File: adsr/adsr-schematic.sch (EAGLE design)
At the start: 28 parts, among them IC1 NE555N, IC2 LM358N, Q1 BC548B, Q2 BC548B, Q3 BC548B

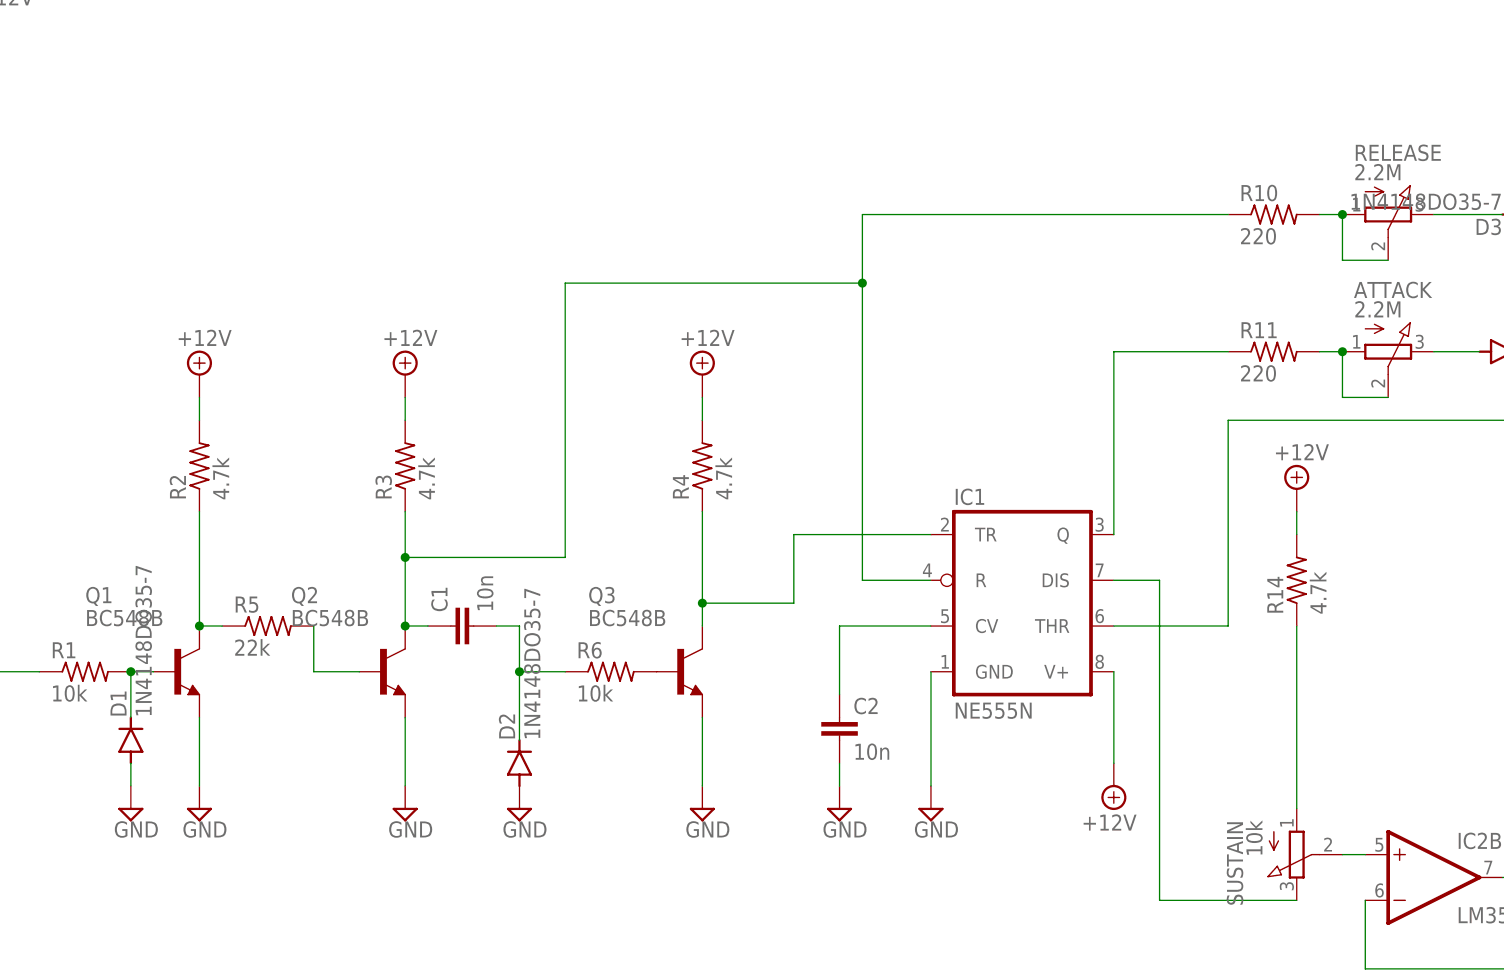
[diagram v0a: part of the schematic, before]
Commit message: save sequencer and adsr.
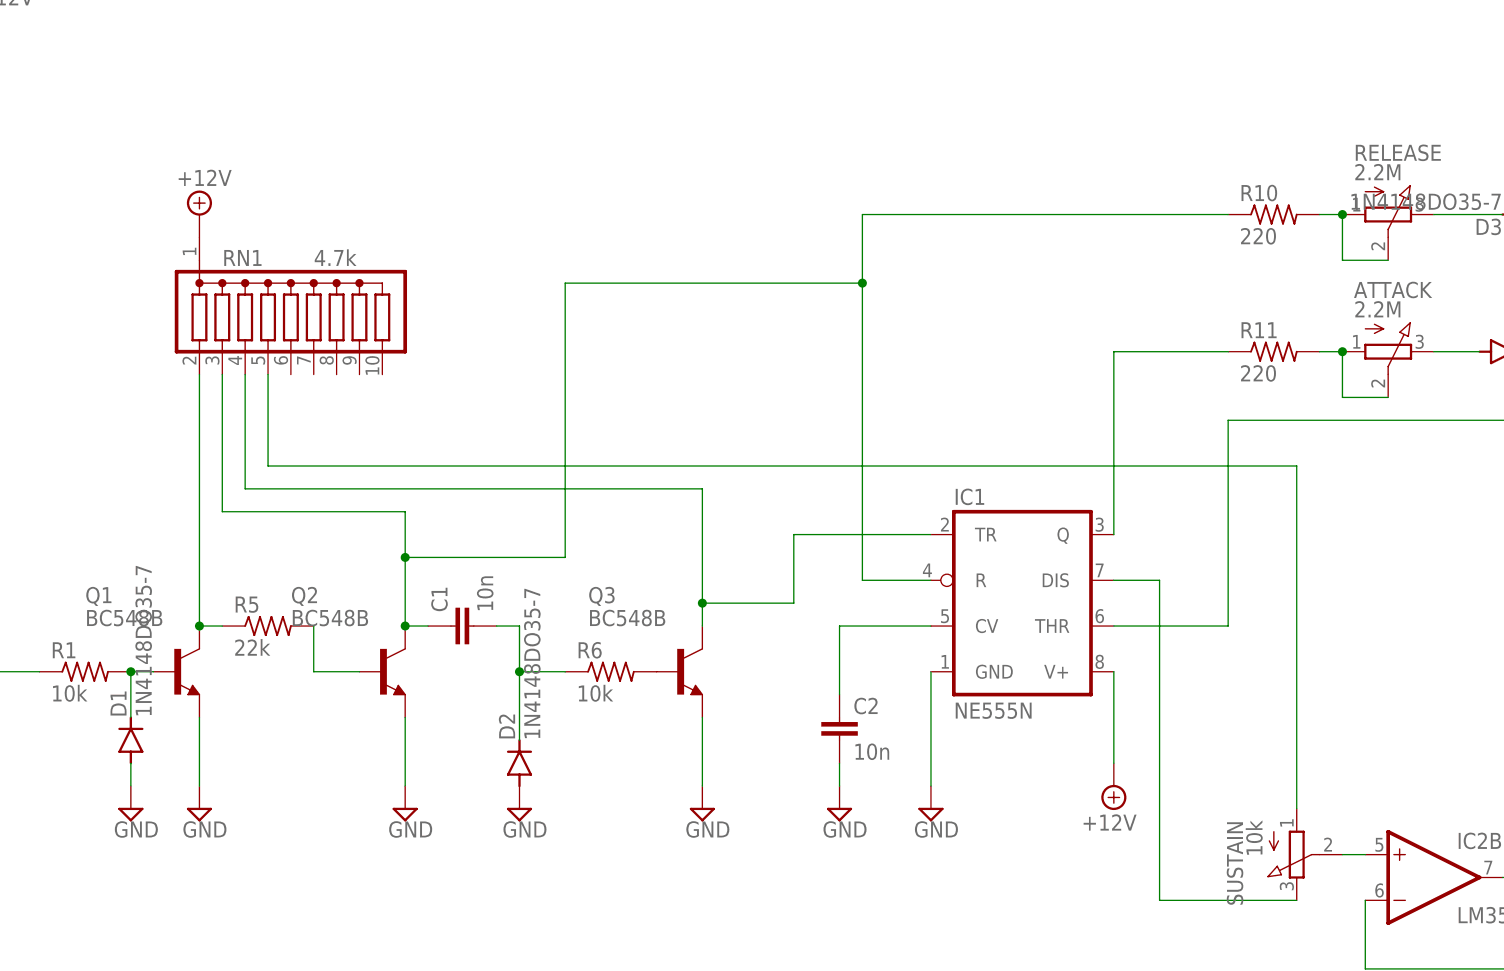
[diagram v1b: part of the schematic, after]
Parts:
- removed R14, R2, R3, R4: 4.7k, rcl:R-US_0204/5
- added RN1: 4.7k, resistor-sil:G09R
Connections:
- net +12V: now also RN1.1; no longer R14.2, R2.2, R3.2, R4.2
- net N$17: now also RN1.5; no longer R14.1
- net N$2: now also RN1.2; no longer R2.1
- net N$3: now also RN1.3; no longer R3.1
- net N$4: now also RN1.4; no longer R4.1
